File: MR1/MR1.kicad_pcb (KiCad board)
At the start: 2 copper layers, 4.5 x 3.5 mm, 97 parts, among them J1 Conn_Coaxial, J2 Conn_Coaxial, J22 B4B_PH, J23 Jumper_1, J3 USB_C_Receptacle_USB2.0, J36 Conn_ARM_JTAG_SWD_10, J4 Conn_Coaxial, J5 Conn_01x05_Socket, J6 Conn_01x05_Socket, U1 LM27762, U12 ADR4550, U13 ADR4550, U2 LMP7721, U3 OP07, U33 NCP163ASN330T1G, U34 NCP163ASN330T1G, U4 LT3045xDD, U5 LT3094xDD, U7 SN65220, U8 ESP32-S3-MINI-1U, U9 MCP4822, Y2 32.768 kHz

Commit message: Signed-off-by: lokimetasmith <lokimail@gmail.com>
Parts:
- removed C46, C47: 0.1u, Capacitor_SMD:C_0603_1608Metric
- removed J2: Conn_Coaxial, Connector_Coaxial:MMCX_Molex_73415-0961_Horizontal_1.0mm-PCB
- removed R8: 100K, Resistor_SMD:R_0402_1005Metric
- added R10: 1K, Resistor_SMD:R_0402_1005Metric, F.Cu at (71.2, 132.4)
- added R13: 1K, Resistor_SMD:R_0402_1005Metric, F.Cu at (71.2, 134.6)
- added R27: 1K, Resistor_SMD:R_0402_1005Metric, F.Cu at (71.2, 136.3)
- added R28: 1K, Resistor_SMD:R_0402_1005Metric, F.Cu at (71.2, 138.3)
- added U14: TMUX1108RSV, Package_DFN_QFN:UQFN-16_1.8x2.6mm_P0.4mm, F.Cu at (74.7, 133.8)
- C1, C10, C118, C119, C120, C121, C13, C14, C15, C18, C2, C3, C4, C5, C6, C7: footprint Capacitor_SMD:C_0805_2012Metric -> Capacitor_SMD:C_0402_1005Metric
- C11, C12, C43, C44, C45, C75, C8, C9: footprint Capacitor_SMD:C_0603_1608Metric -> Capacitor_SMD:C_0402_1005Metric
- C16, C17: footprint Capacitor_SMD:C_1206_3216Metric -> Capacitor_SMD:C_0402_1005Metric
- R1: footprint Resistor_SMD:R_1206_3216Metric -> Resistor_SMD:R_0402_1005Metric
- R19, R2, R20, R21, R22, R3, R31, R35, R39, R4, R40, R5, R6, R7: footprint Resistor_SMD:R_0805_2012Metric -> Resistor_SMD:R_0402_1005Metric
- moved R23 236.7 mm to (97.6, 161.7), turned to 90 degrees
- moved C18 232.5 mm to (128.8, 167.7)
- moved J5 232.5 mm to (96.2, 173.5)
- moved R19 232.5 mm to (111.6, 161.1)
- moved R22 232.5 mm to (124.3, 182.4)
- moved R26 232.5 mm to (102.0, 147.8)
- moved C13 232.5 mm to (104.1, 162.2)
- moved C14 232.5 mm to (99.6, 166.7)
- moved C15 232.5 mm to (105.1, 158.7)
- moved R18 232.5 mm to (100.1, 164.7)
- moved R20 232.5 mm to (124.3, 176.5)
- moved R21 232.5 mm to (124.3, 179.5)
- moved R24 232.5 mm to (99.1, 157.7)
- moved R7 232.5 mm to (124.3, 170.6)
- moved U1 232.5 mm to (100.1, 162.5)
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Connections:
- R15 pad 2: /USB_D+ -> /GPIO20
- R16 pad 2: /USB_D- -> /GPIO19
- U8 pad 23: /D- -> /GPIO19
- U8 pad 24: /D+ -> /GPIO20
- U9 pad 4: SDI -> CS_
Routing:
- net Net-(U1-OUT-): track 0.00 -> 15.4 mm
- net GNDA: track 0.00 -> 6.79 mm
- net Net-(U1-OUT+): track 0.00 -> 6.01 mm
- net Net-(U14-S1): track 0.00 -> 2.93 mm
- net Net-(U1-PGOOD): track 0.00 -> 1.57 mm
- net VBUS: track 0.00 -> 1.55 mm

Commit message: Signed-off-by: lokimetasmith <lokimail@gmail.com>
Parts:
- removed J4: Conn_Coaxial, Connector_Coaxial:MMCX_Molex_73415-0961_Horizontal_1.0mm-PCB
- removed J5: Conn_01x05_Socket, Connector_JST:JST_PH_B5B-PH-K_1x05_P2.00mm_Vertical
- removed J6: Conn_01x05_Socket, Connector_JST:JST_PH_S5B-PH-K_1x05_P2.00mm_Horizontal
- removed R2: 100, Resistor_SMD:R_0402_1005Metric
- added J10: Conn_01x01_Pin, footprints:Electrode, B.Cu at (150.4, 65.5)
- added J11: Conn_01x01_Pin, footprints:Electrode, B.Cu at (156.4, 62.0)
- added J12: Conn_01x10, Connector_JST:JST_SH_SM10B-SRSS-TB_1x10-1MP_P1.00mm_Horizontal, F.Cu at (76.0, 144.7)
- added J2: Conn_01x01_Pin, footprints:Electrode, F.Cu at (177.6, 67.2)
- added J9: Conn_01x10, Connector_JST:JST_SH_SM10B-SRSS-TB_1x10-1MP_P1.00mm_Horizontal, F.Cu at (164.5, 78.6)
- added NT4: NetTie_2, NetTie:NetTie-2_SMD_Pad0.5mm, F.Cu at (183.1, 94.9)
- added R8: 100, Resistor_SMD:R_0402_1005Metric, F.Cu at (165.0, 74.3)
- J1: value Conn_Coaxial -> Conn_01x01_Pin; footprint Connector_Coaxial:MMCX_Molex_73415-0961_Horizontal_1.0mm-PCB -> footprints:Electrode
- U14: value TMUX1108RSV -> TMUX1104dgsr; footprint Package_DFN_QFN:UQFN-16_1.8x2.6mm_P0.4mm -> Package_SO:VSSOP-10_3x3mm_P0.5mm
- moved U3 131.1 mm to (91.0, 183.7)
- moved R5 116.6 mm to (98.0, 175.5)
- moved R3 112.3 mm to (96.5, 173.8), turned to 180 degrees
- moved R4 111.4 mm to (107.0, 171.5), turned to 180 degrees
- moved R20 25.6 mm to (99.0, 180.2)
- moved J1 20.5 mm to (171.6, 63.7), turned to 150 degrees
- moved C4 19.3 mm to (168.4, 73.8)
- moved C2 17.2 mm to (168.4, 74.8)
- moved C3 13.6 mm to (166.4, 74.8), turned to 180 degrees
- moved C5 13.5 mm to (166.5, 73.8), turned to 180 degrees
- moved C1 13.0 mm to (169.9, 66.7), turned to 60 degrees
- moved R1 10.9 mm to (169.0, 66.2), turned to 60 degrees
- moved NT3 8.48 mm to (162.3, 68.8)
- moved U2 7.83 mm to (164.8, 70.1)
- moved C6 7.73 mm to (163.5, 74.8)
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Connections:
- C6 pad 1: /Vbias -> /Vbias_AMP
- NT3 pad 2: /Vbias -> /Vbias_AMP
- R3 pad 1: /Signal -> Net-(U6-IN+)
- R35 pad 2: >PORE -> />PORE
- R5 pad 1: Net-(U3-+) -> /Signal_Return
- R6 pad 1: /Vbias -> /Vbias_AMP
- U14 pad 1: unconnected-(U14-VSS-Pad1) -> /GPIO40
- U14 pad 10: unconnected-(U14-S5-Pad10) -> /GPIO41
- U14 pad 3: Net-(U14-S2) -> GNDA
- U14 pad 5: Net-(U14-S4) -> ESP32_VCC_3V3
- U14 pad 6: /Signal -> ESP32_VCC_3V3
- U14 pad 7: unconnected-(U14-S8-Pad7) -> Net-(U14-S4)
- U14 pad 8: unconnected-(U14-S7-Pad8) -> /Signal_Return
- U14 pad 9: unconnected-(U14-S6-Pad9) -> Net-(U14-S2)
- U2 pad 1: /Vbias -> /Vbias_AMP
- U3 pad 3: Net-(U3-+) -> /Signal_Return
- U3 pad 6: /Signal -> Net-(U6-IN+)
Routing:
- net /Vbias_AMP: track 0.00 -> 40.7 mm, vias 0 -> 3
- net GNDA: track 6.79 -> 26.5 mm
- net Net-(C1-Pad1): track 0.00 -> 18.0 mm
- net /SHIELD_AMP: track 0.00 -> 16.2 mm
- net />PORE_AMP: track 0.00 -> 15.3 mm, vias 0 -> 1
- net Net-(J1-Pin_1): track 0.00 -> 9.68 mm
- net VSSA: track 0.00 -> 9.02 mm
- net /GUARD: track 0.00 -> 8.88 mm
- net VDDA: track 0.00 -> 7.81 mm
- net Net-(J2-Pin_1): track 0.00 -> 5.65 mm
- net /Signal_AMP: track 0.00 -> 1.84 mm
- added copper zone on F.Cu, net GNDA
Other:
- board size 4.5 x 3.5 mm -> 60 x 52 mm

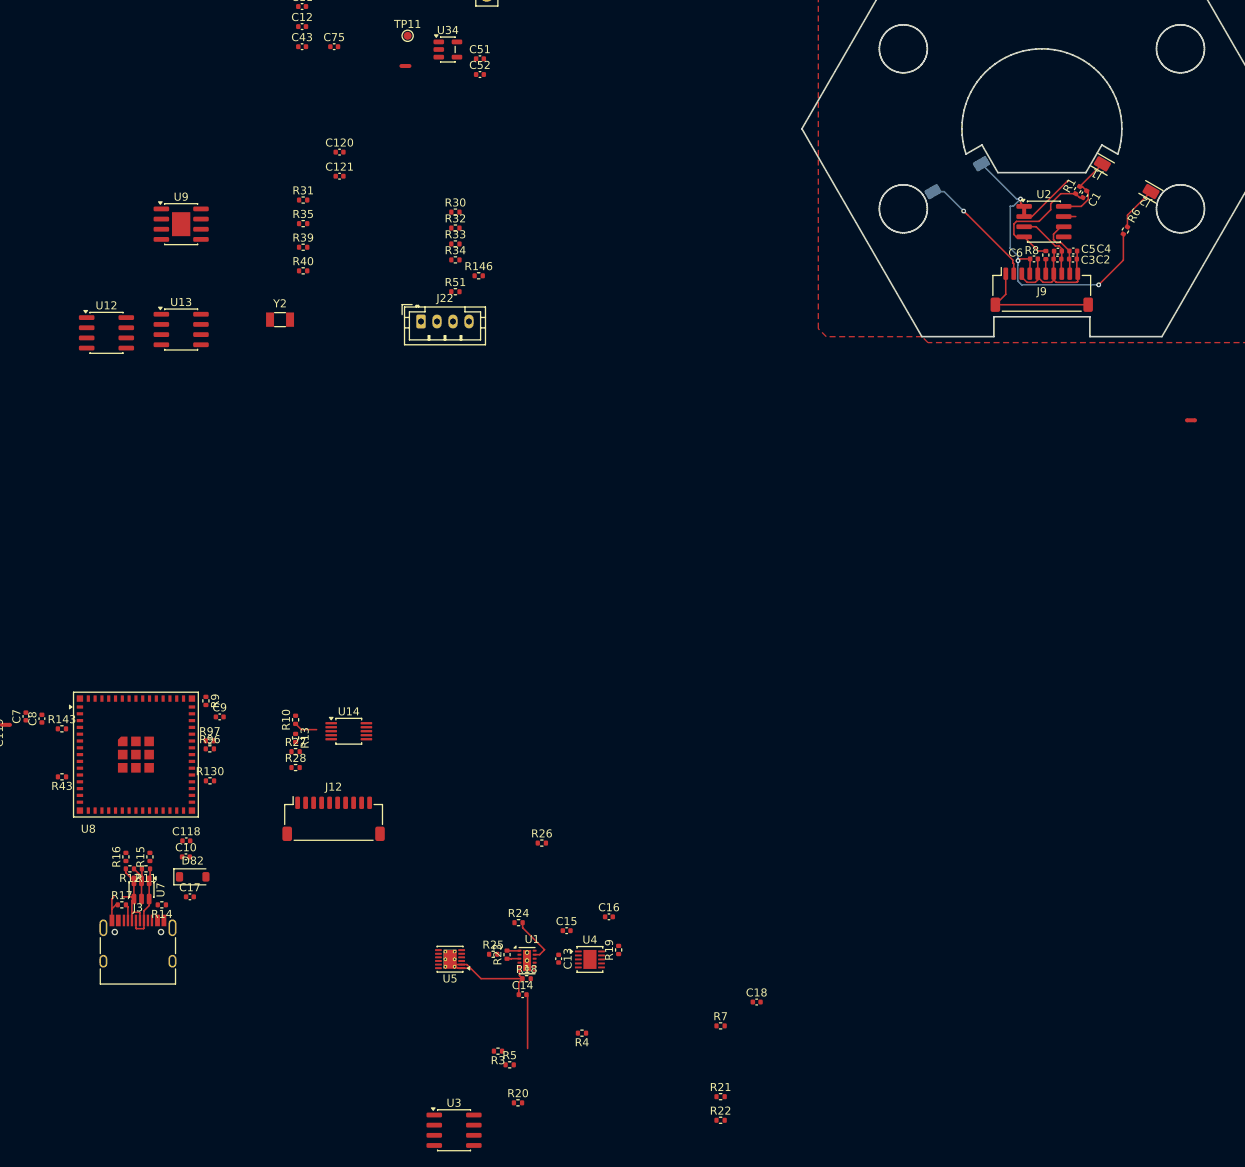
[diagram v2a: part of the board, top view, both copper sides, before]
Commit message: added nanopore depression, updated cad
Signed-off-by: lokimetasmith <lokimail@gmail.com>
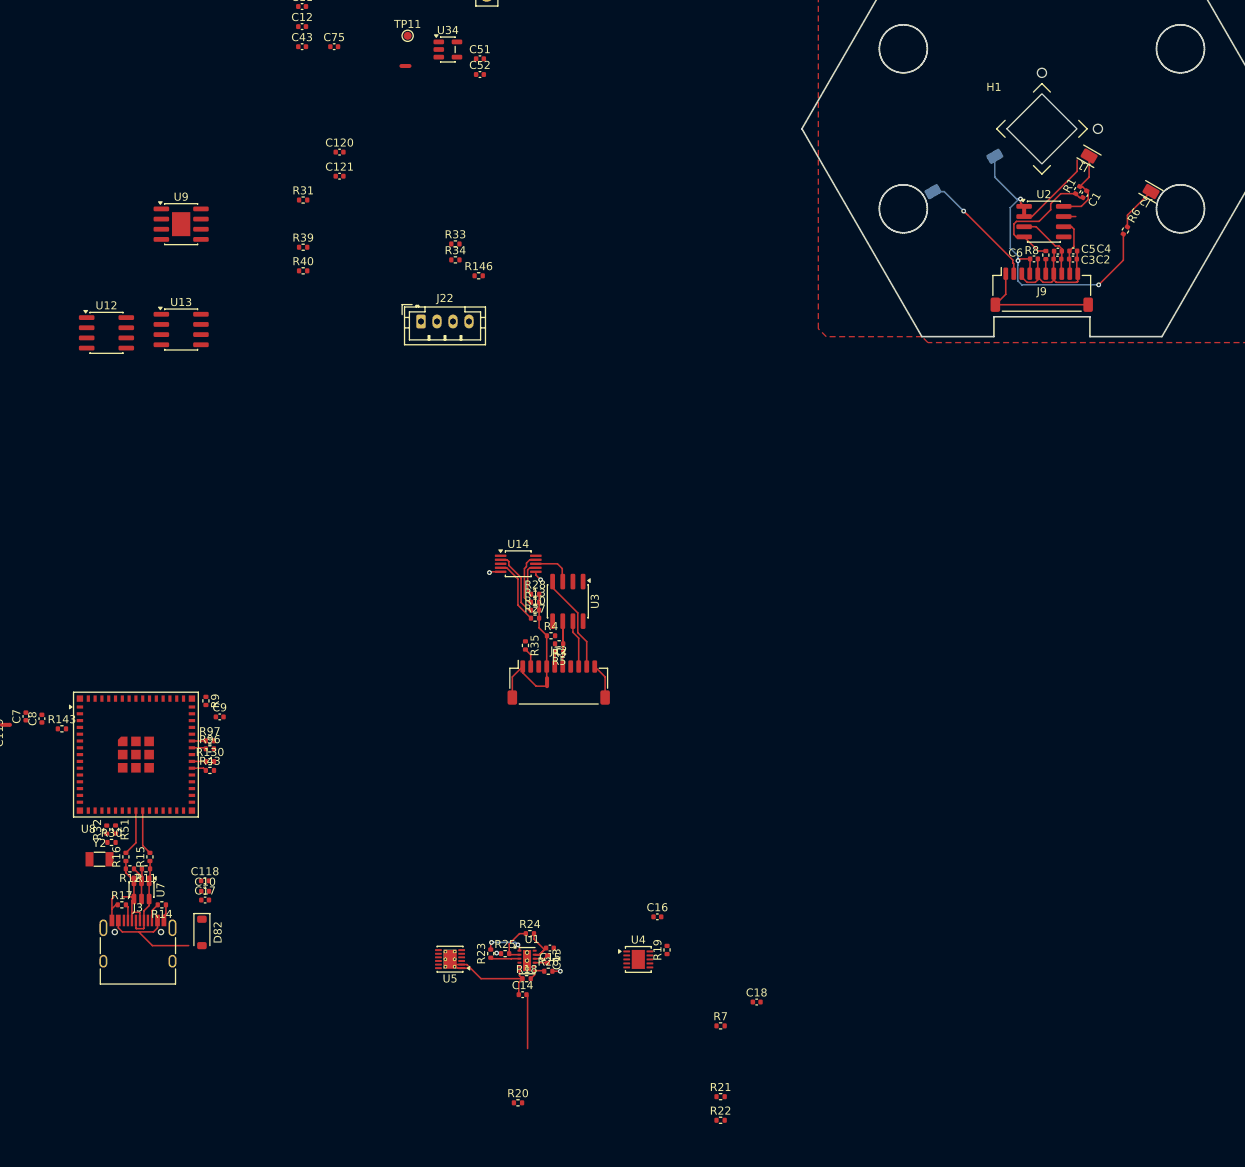
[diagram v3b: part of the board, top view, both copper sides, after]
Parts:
- added H1: Nanopore, footprints:Nanopore holder_recessed, F.Cu at (164.5, 58.5)
- moved R30 89.8 mm to (48.2, 147.7)
- moved R32 86.9 mm to (47.6, 146.1), turned to 90 degrees
- moved NT4 86.9 mm to (102.6, 127.7), turned to -90 degrees
- moved R51 79.5 mm to (48.7, 146.1), turned to -90 degrees
- moved Y2 71.1 mm to (46.7, 149.8)
- moved U3 67.6 mm to (105.2, 117.6), turned to -90 degrees
- moved R35 59.6 mm to (99.9, 123.1), turned to -90 degrees
- moved R5 52.0 mm to (104.1, 123.9), turned to 180 degrees
- moved R3 51.5 mm to (104.2, 122.9)
- moved R4 49.8 mm to (103.1, 121.9), turned to 0 degrees
- moved R28 37.0 mm to (101.2, 116.7)
- moved R13 34.4 mm to (101.1, 117.7), turned to 0 degrees
- moved R27 34.3 mm to (101.1, 119.7)
- moved R10 32.9 mm to (101.1, 118.7), turned to 0 degrees
- moved J12 32.9 mm to (104.1, 127.7)
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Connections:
- net /DIN renamed /GPIO18
- net /Fan_EN renamed /GPIO11
- J12 pad 2: /Signal_Return -> />PORE
- J12 pad 4: VSSA -> /Vbias
- J12 pad 5: VDDA -> GNDA
- J12 pad 6: GNDA -> /Signal_Return
- J12 pad 7: />PORE -> GNDA
- J12 pad 8: GNDA -> VSSA
- J12 pad 9: /Vbias -> VDDA
- R10 pad 2: Net-(R10-Pad2) -> /Vbias
- R13 pad 2: Net-(R10-Pad2) -> /Vbias
- R130 pad 1: /GPIO38 -> /GPIO41
- R130 pad 2: unconnected-(R130-Pad2) -> /TMUX_A1
- R27 pad 2: Net-(R10-Pad2) -> /Vbias
- R28 pad 2: Net-(R10-Pad2) -> /Vbias
- R3 pad 1: Net-(U6-IN+) -> /Signal_Return
- R39 pad 1: unconnected-(R39-Pad1) -> Net-(U9-VB)
- R43 pad 1: /GPIO7 -> /GPIO40
- R43 pad 2: unconnected-(R43-Pad2) -> /TMUX_A0
- U14 pad 1: /GPIO40 -> /TMUX_A0
- U14 pad 10: /GPIO41 -> /TMUX_A1
- U3 pad 6: Net-(U6-IN+) -> /Signal_Return
- U8 pad 16: unconnected-(U8-IO12-Pad16) -> /GPIO12
- U8 pad 17: unconnected-(U8-IO13-Pad17) -> /GPIO13
- U8 pad 18: unconnected-(U8-IO14-Pad18) -> /GPIO14
- U8 pad 9: unconnected-(U8-IO5-Pad9) -> /GPIO5
- U9 pad 6: unconnected-(U9-VB-Pad6) -> Net-(U9-VB)
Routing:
- net /V_USB: track 0.00 -> 14.1 mm
- net /Signal_Return: track 0.00 -> 13.8 mm
- net /SHIELD: track 0.00 -> 13.3 mm
- net VDDA: track 7.81 -> 19.6 mm
- net /Vbias: track 0.00 -> 10.9 mm
- net Net-(U14-S3): track 0.00 -> 8.31 mm
- net Net-(U14-S2): track 0.00 -> 6.83 mm
- net VSSA: track 9.02 -> 15.0 mm
- net /GPIO19: track 0.00 -> 5.80 mm
- net /GPIO20: track 0.00 -> 5.65 mm
- net Net-(U14-S1): track 2.93 -> 8.50 mm
- net Net-(U1-FB+): track 0.00 -> 5.16 mm
- net Net-(U14-S4): track 0.00 -> 4.35 mm
- net Net-(U1-PGOOD): track 1.57 -> 5.16 mm, vias 0 -> 2
- net GNDA: track 26.5 -> 30.0 mm, vias 0 -> 2
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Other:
- outline, holes or cut-outs redrawn

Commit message: Signed-off-by: lokimetasmith <lokimail@gmail.com>
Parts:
- added C19: 100nF, Capacitor_SMD:C_0402_1005Metric, F.Cu at (104.6, 112.2)
- added C20: 100nF, Capacitor_SMD:C_0402_1005Metric, F.Cu at (106.9, 112.2)
- added U16: LTC6268xS8-10, Package_SO:SO-8_3.9x4.9mm_P1.27mm, F.Cu at (105.1, 116.7)
- U3: value OP07 -> ADS127L01xPBS; footprint Package_SO:SOIC-8_3.9x4.9mm_P1.27mm -> Package_QFP:TQFP-32_5x5mm_P0.5mm
- moved U3 21.8 mm to (117.1, 99.3)
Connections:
- C44 pad 1: GND -> unconnected-(C44-Pad1)
- C44 pad 2: /ANA_1 -> unconnected-(C44-Pad2)
- C75 pad 2: /ANA_3 -> unconnected-(C75-Pad2)
- J12 pad 10: /SHIELD -> GNDA
- R3 pad 1: /Signal_Return -> Net-(U6-IN+)
- R3 pad 2: Net-(U3--) -> Net-(U16--)
- R4 pad 2: Net-(U3--) -> Net-(U16--)
- U3 pad 2: Net-(U3--) -> unconnected-(U3-CAP1-Pad2)
- U3 pad 3: /Signal_Return -> unconnected-(U3-AINN-Pad3)
- U3 pad 4: VDDA -> unconnected-(U3-AINP-Pad4)
- U3 pad 5: unconnected-(U3-NC-Pad5) -> Net-(U3-AGND-Pad31)
- U3 pad 6: /Signal_Return -> Net-(U3-AVDD-Pad32)
- U3 pad 7: VSSA -> unconnected-(U3-REXT-Pad7)
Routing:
- net /Vbias: track 10.9 -> 28.4 mm
- net Net-(U6-IN+): track 0.00 -> 9.19 mm
- net GNDA: track 30.0 -> 39.1 mm, vias 2 -> 7
- net /Signal_Return: track 13.8 -> 6.91 mm
- net /SHIELD: track 13.3 -> 8.92 mm
- net Net-(U16--): track 0.00 -> 3.93 mm
- net VSSA: track 15.0 -> 16.8 mm, vias 0 -> 2
- net VDDA: vias 0 -> 2
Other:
- copper layers 2 -> 6

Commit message: Signed-off-by: lokimetasmith <lokimail@gmail.com>
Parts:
- removed C43, C44, C45, C75: 0.1u, Capacitor_SMD:C_0402_1005Metric
- removed R39: 1000, Resistor_SMD:R_0402_1005Metric
- removed U3: ADS127L01xPBS, Package_QFP:TQFP-32_5x5mm_P0.5mm
- added C21: 22u, Capacitor_SMD:C_0402_1005Metric, F.Cu at (80.6, 140.5)
- added C22: 22u, Capacitor_SMD:C_0402_1005Metric, F.Cu at (80.6, 142.5)
- added C23: 4.7u, Capacitor_SMD:C_0402_1005Metric, F.Cu at (80.6, 144.4)
- added R2: 24.9k 0.1%, Resistor_SMD:R_0402_1005Metric, F.Cu at (83.5, 140.5)
- added R29: 10k 1%, Resistor_SMD:R_0402_1005Metric, F.Cu at (83.5, 142.5)
- C8: value 0.1u -> 4.7u
- R19: value 5k -> 9.16k
- R20: value 5k -> 9.09k
- R21, R22: value 5k -> 10k 1%
- R31: value 1000 -> 3K9
- R7: value 5k -> 24.9k 0.1%
- U4: footprint Package_DFN_QFN:DFN-10-1EP_3x3mm_P0.5mm_EP1.65x2.38mm -> Package_DFN_QFN:DFN-12-1EP_3x3mm_P0.5mm_EP1.6x2.5mm
- moved C6 7.80 mm to (161.3, 67.3)
- moved C5 6.95 mm to (162.3, 68.3)
- moved C3 6.59 mm to (162.1, 69.8)
- moved NT3 4.08 mm to (165.6, 66.4), turned to 60 degrees
- moved U2 2.96 mm to (167.5, 69.0), turned to -30 degrees
- moved C4 2.80 mm to (171.1, 72.8), turned to 180 degrees
- moved C2 2.78 mm to (171.1, 74.0), turned to 180 degrees
- moved R6 2.36 mm to (172.6, 71.0)
- moved R1 1.30 mm to (169.5, 65.0), turned to -30 degrees
- moved C1 1.29 mm to (168.9, 65.8), turned to -30 degrees
- moved R8 0.99 mm to (164.0, 74.3)
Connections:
- C119 pad 1: Net-(U33-VOUT) -> Net-(U8-3V3)
- C14 pad 1: Net-(U1-OUT-) -> /-Vp
- C15 pad 2: Net-(U1-OUT+) -> /+Vp
- C8 pad 1: Net-(U8-3V3) -> GNDA
- C8 pad 2: GND -> Net-(U4-SET)
- J12 pad 1: /SHIELD -> />PORE
- J12 pad 10: GNDA -> /SHIELD
- J12 pad 2: />PORE -> GNDA
- J12 pad 3: GNDA -> /Vbias
- J12 pad 4: /Vbias -> /SHIELD
- J12 pad 5: GNDA -> /Signal_Return
- J12 pad 6: /Signal_Return -> GNDA
- J12 pad 7: GNDA -> VSSA
- J12 pad 8: VSSA -> VDDA
- J12 pad 9: VDDA -> /SHIELD
- J9 pad 1: /SHIELD_AMP -> />PORE_AMP
- J9 pad 10: GNDA -> /SHIELD_AMP
- J9 pad 2: />PORE_AMP -> GNDA
- J9 pad 3: GNDA -> /Vbias_AMP
- J9 pad 4: /Vbias_AMP -> /SHIELD_AMP
- J9 pad 5: GNDA -> /Signal_AMP
- J9 pad 6: /Signal_AMP -> GNDA
- J9 pad 7: GNDA -> VDDA
- J9 pad 9: VDDA -> /SHIELD_AMP
- R18 pad 1: Net-(U1-OUT-) -> /-Vp
- R18 pad 2: Net-(U1-FB-) -> /FB-
- R19 pad 1: VDDA -> /+VIOC
- R19 pad 2: Net-(U4-OUT) -> /FB+
- R20 pad 1: GNDA -> /-VIOC
- R20 pad 2: VDDA -> /FB-
- R21 pad 1: VSSA -> Net-(U11--)
- R21 pad 2: Net-(R21-Pad2) -> Net-(U9-VB)
- R22 pad 1: GNDA -> Net-(U11--)
- R22 pad 2: VSSA -> Net-(U12-OUT)
- R24 pad 1: Net-(U1-FB+) -> /FB+
- R24 pad 2: Net-(U1-OUT+) -> /+Vp
- R25 pad 2: Net-(U1-FB+) -> /FB+
- R26 pad 1: Net-(U1-FB-) -> /FB-
- R35 pad 1: Net-(U10-+) -> Net-(U13-OUT)
- R35 pad 2: />PORE -> Net-(U10-+)
- R7 pad 1: unconnected-(R7-Pad1) -> Net-(U5-SET)
- R7 pad 2: unconnected-(R7-Pad2) -> GNDA
- U1 pad 11: Net-(U1-OUT+) -> /+Vp
- U1 pad 12: unconnected-(U1-EN+-Pad12) -> Net-(U1-EN+)
- U1 pad 2: Net-(U1-FB+) -> /FB+
- U1 pad 6: Net-(U1-OUT-) -> /-Vp
- U1 pad 7: Net-(U1-FB-) -> /FB-
- U1 pad 8: unconnected-(U1-EN--Pad8) -> Net-(U1-EN+)
- U12 pad 6: Net-(U11--) -> Net-(U12-OUT)
- U13 pad 6: Net-(U10-+) -> Net-(U13-OUT)
- U4 pad 1: Net-(U1-OUT+) -> /+Vp
- U4 pad 10: Net-(U4-OUT) -> unconnected-(U4-OUTS-Pad10)
- U4 pad 2: Net-(U1-OUT+) -> /+Vp
- U4 pad 3: unconnected-(U4-EN/UV-Pad3) -> /+VIOC
- U4 pad 4: unconnected-(U4-PG-Pad4) -> /+Vp
- U4 pad 6: unconnected-(U4-PGFB-Pad6) -> GNDA
- U4 pad 7: unconnected-(U4-SET-Pad7) -> /+Vp
- U4 pad 8: GNDA -> Net-(U4-SET)
- U4 pad 9: VDDA -> GNDA
- U5 pad 1: Net-(U1-OUT-) -> /-Vp
- U5 pad 11: Net-(R21-Pad2) -> VSSA
- U5 pad 12: Net-(R21-Pad2) -> VSSA
- U5 pad 13: Net-(U1-OUT-) -> /-Vp
- U5 pad 2: Net-(U1-OUT-) -> /-Vp
- U5 pad 3: unconnected-(U5-EN/UV-Pad3) -> /-Vp
- U5 pad 5: unconnected-(U5-PGFB-Pad5) -> /-Vp
- U5 pad 6: unconnected-(U5-ILIM-Pad6) -> GNDA
- U5 pad 7: unconnected-(U5-VIOC-Pad7) -> /-VIOC
- U5 pad 8: unconnected-(U5-SET-Pad8) -> Net-(U5-SET)
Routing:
- net Net-(U1-OUT-): track 15.4 -> 0.00 mm
- net /-Vp: track 0.00 -> 15.4 mm
- net /Vbias_AMP: track 40.9 -> 30.9 mm, vias 3 -> 4
- net VSSA: track 16.8 -> 24.8 mm, vias 2 -> 4
- net VDDA: track 19.6 -> 26.5 mm
- net GNDA: track 39.1 -> 33.0 mm, vias 7 -> 4
- net Net-(C1-Pad1): track 18.0 -> 11.8 mm
- net Net-(U1-OUT+): track 5.83 -> 0.00 mm
- net /+Vp: track 0.00 -> 5.83 mm
- net Net-(U1-FB+): track 5.16 -> 0.00 mm
- net /FB+: track 0.00 -> 5.16 mm
- net /SHIELD_AMP: track 16.2 -> 20.7 mm
- net /GUARD: track 11.9 -> 8.11 mm
- net /SHIELD: track 8.92 -> 12.4 mm, vias 0 -> 2
- net Net-(U1-FB-): track 2.43 -> 0.00 mm
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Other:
- board size 60 x 52 mm -> 8.8 x 8.8 mm
